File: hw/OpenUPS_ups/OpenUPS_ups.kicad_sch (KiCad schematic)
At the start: 5 parts, among them J101 XT60PW-M, U101 AVR32DB28x-xSO

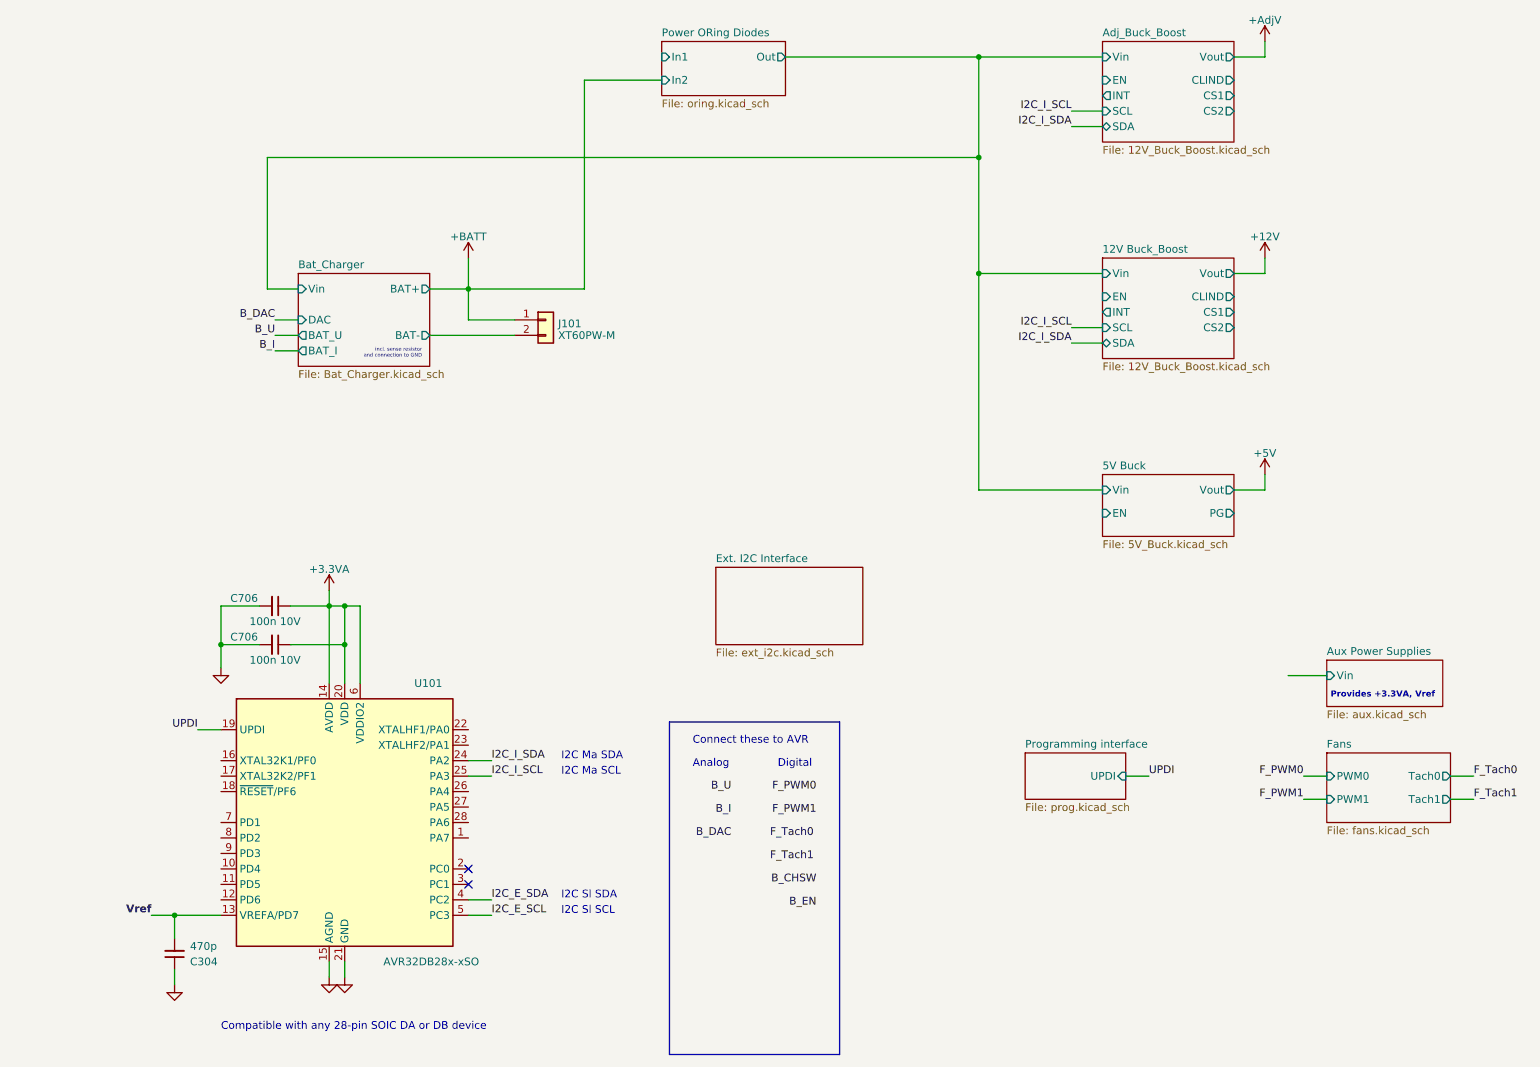
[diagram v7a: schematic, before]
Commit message: External I2C isolator
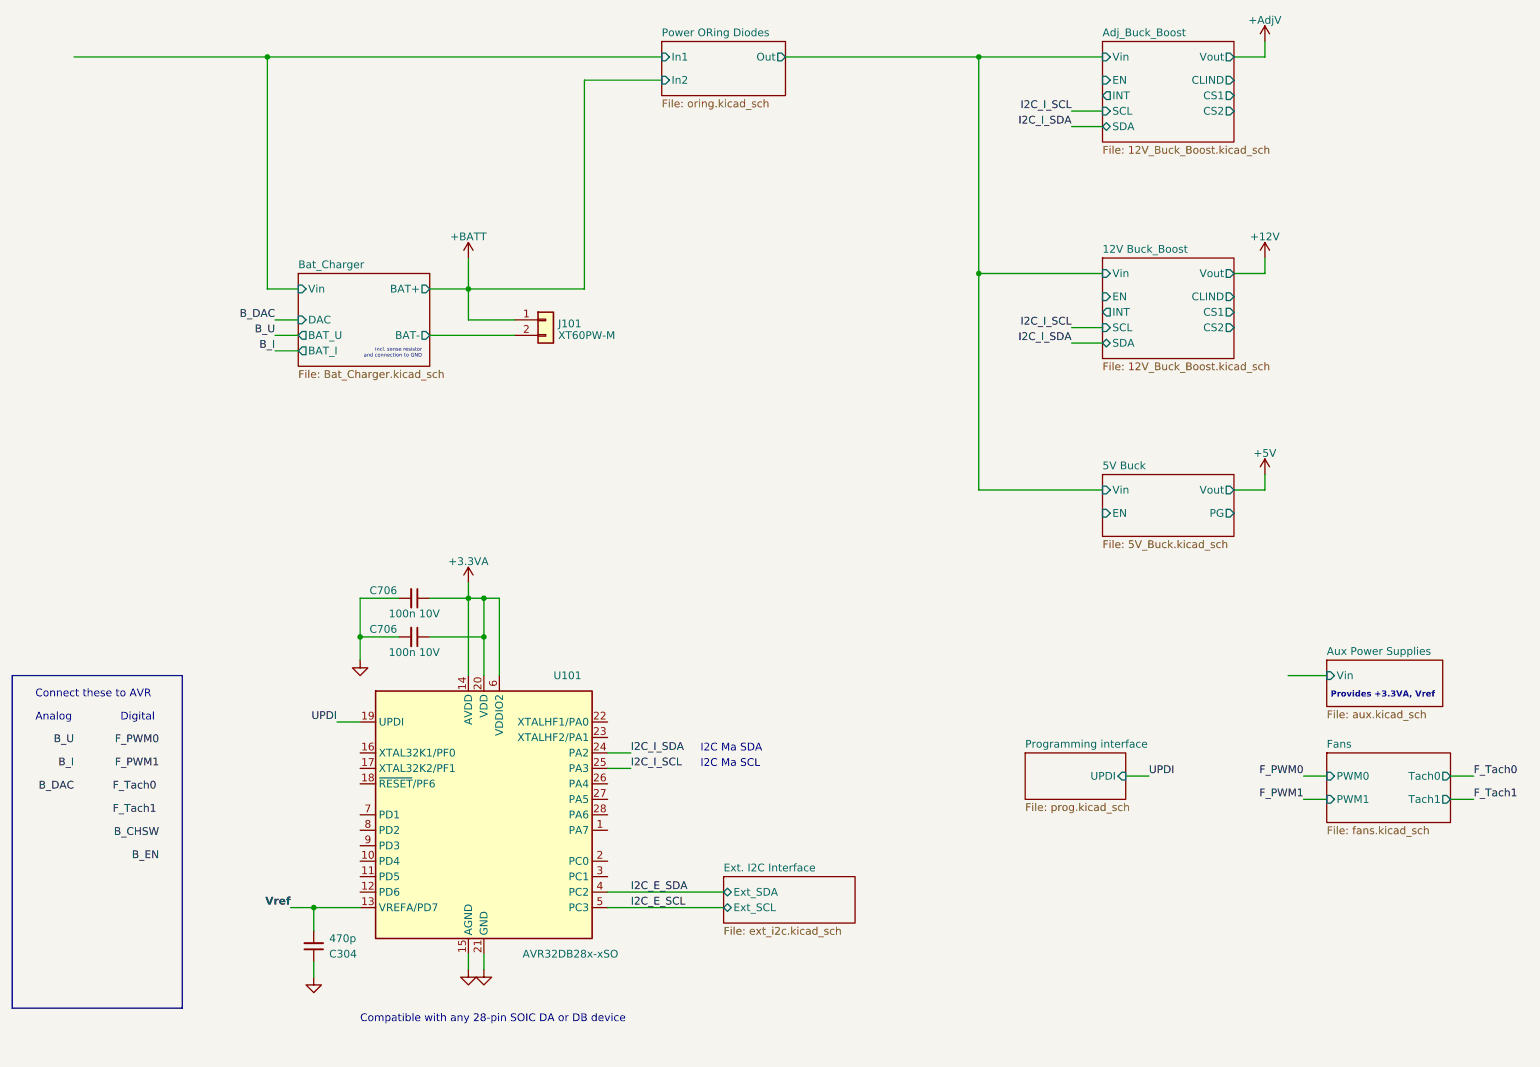
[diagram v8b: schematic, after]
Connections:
- no-connect marks 2 -> 0
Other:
- sheet Ext. I2C Interface ports: added Ext_SCL, Ext_SDA; removed none
- note removed: "I2C Sl SCL"
- note removed: "I2C Sl SDA"
- moved on the sheet: C304, C706, U101
